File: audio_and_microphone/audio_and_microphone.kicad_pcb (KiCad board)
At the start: 2 copper layers, 17 x 15.5 mm, 12 parts

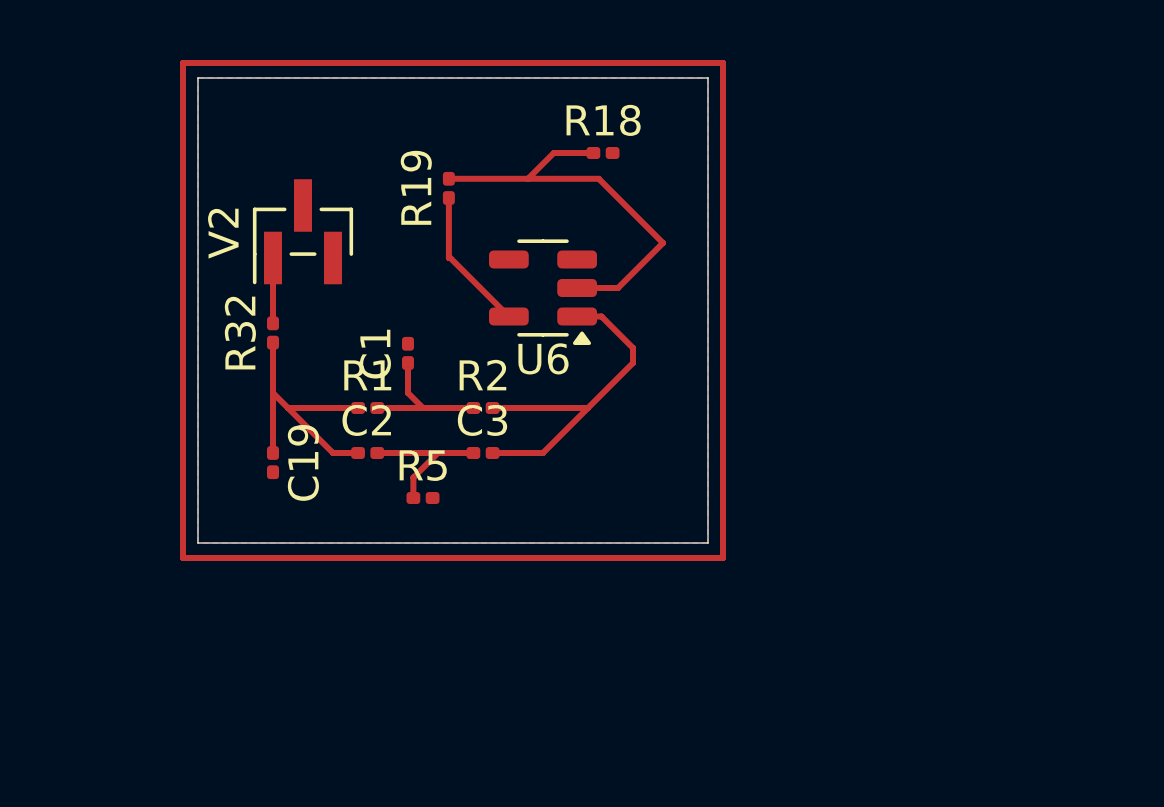
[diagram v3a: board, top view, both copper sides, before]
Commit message: pcb update with pin connectors
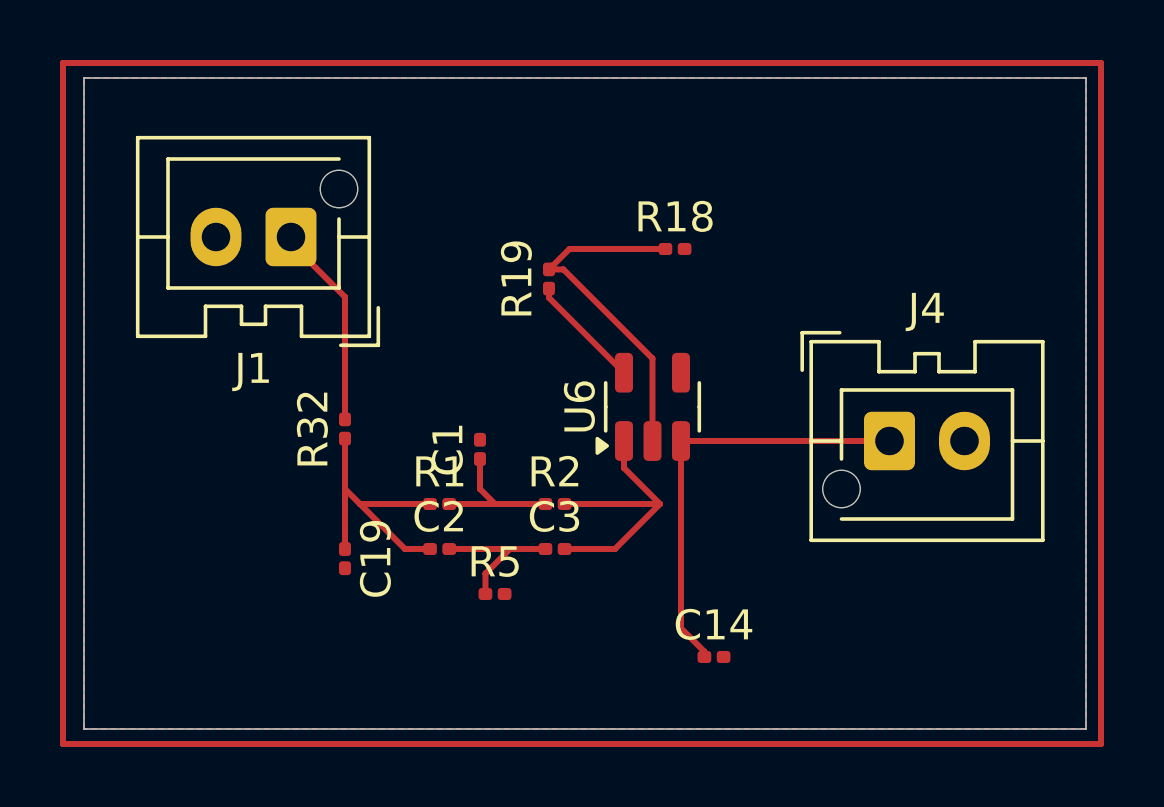
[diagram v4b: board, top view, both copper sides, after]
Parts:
- removed V2: VPWL, Connector_PinHeader_1.00mm:PinHeader_1x03_P1.00mm_Vertical_SMD_Pin1Left
- added C14: 0.1u, Capacitor_SMD:C_0201_0603Metric, F.Cu at (137.7, 64.8)
- added J1: Conn_01x02_Pin, Connector_JST:JST_XA_B02B-XASK-1-A_1x02_P2.50mm_Vertical, F.Cu at (123.6, 50.8)
- added J4: Conn_01x02_Pin, Connector_JST:JST_XA_B02B-XASK-1-A_1x02_P2.50mm_Vertical, F.Cu at (143.6, 57.6)
- moved U6 5.39 mm to (135.7, 56.5), turned to 90 degrees
- moved R19 4.50 mm to (132.2, 52.2)
- moved C1 4.00 mm to (129.9, 57.9)
- moved C19 4.00 mm to (125.4, 61.5)
- moved C2 4.00 mm to (128.6, 61.2)
- moved C3 4.00 mm to (132.4, 61.2)
- moved R1 4.00 mm to (128.6, 59.7)
- moved R18 4.00 mm to (136.4, 51.2)
- moved R2 4.00 mm to (132.4, 59.7)
- moved R32 4.00 mm to (125.4, 57.2)
- moved R5 4.00 mm to (130.4, 62.7)
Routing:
- net +3V3: track 0.00 -> 14.5 mm
- net Net-(J1-Pin_1): track 2.18 -> 6.83 mm
- net Net-(U6--): track 14.0 -> 11.6 mm
- net Net-(U6-+): track 11.9 -> 9.58 mm
- net /ENV_OUT: track 4.81 -> 3.84 mm
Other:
- board size 17 x 15.5 mm -> 33.4 x 21.7 mm

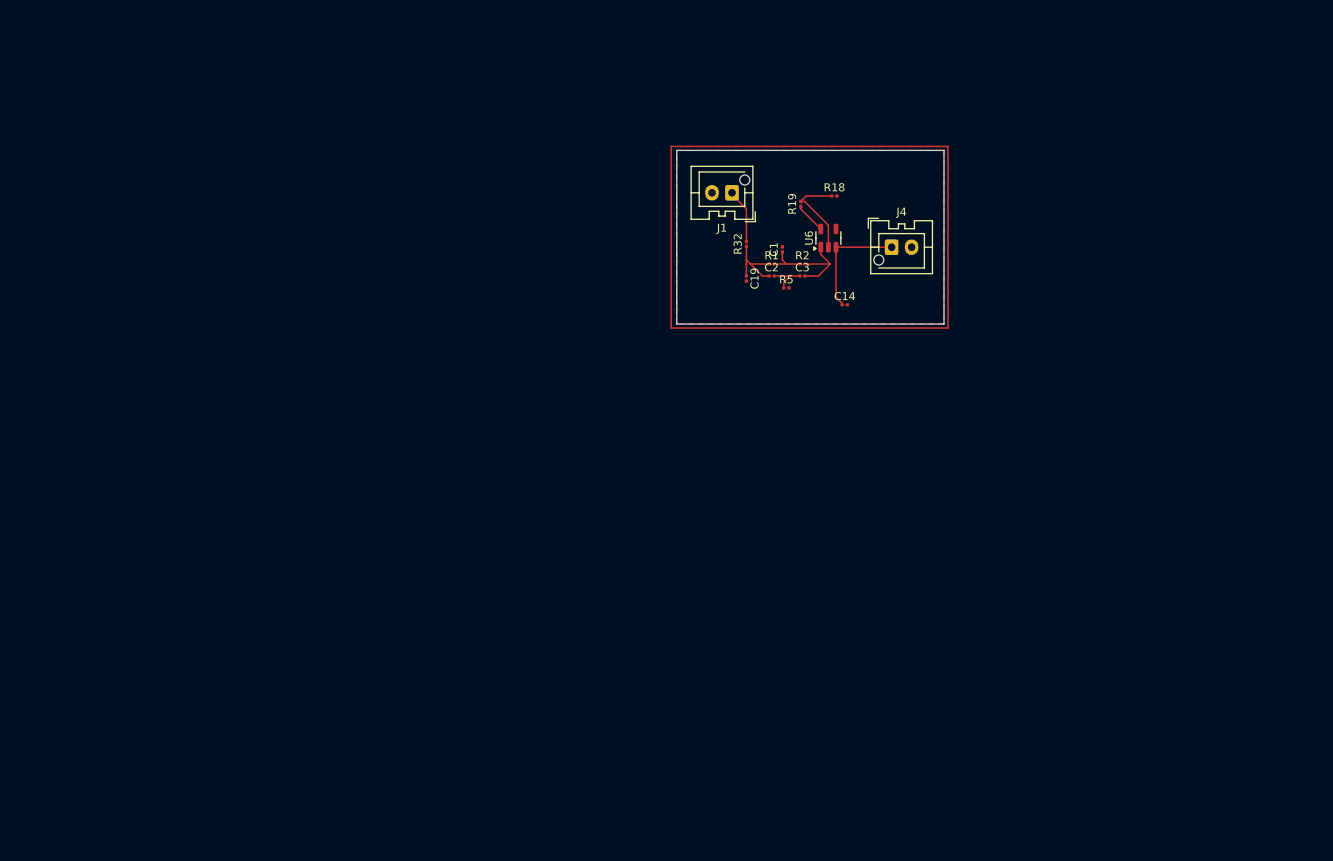
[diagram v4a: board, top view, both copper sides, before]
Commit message: pcb with vertical and horizontal male header pins lined up with arduino size
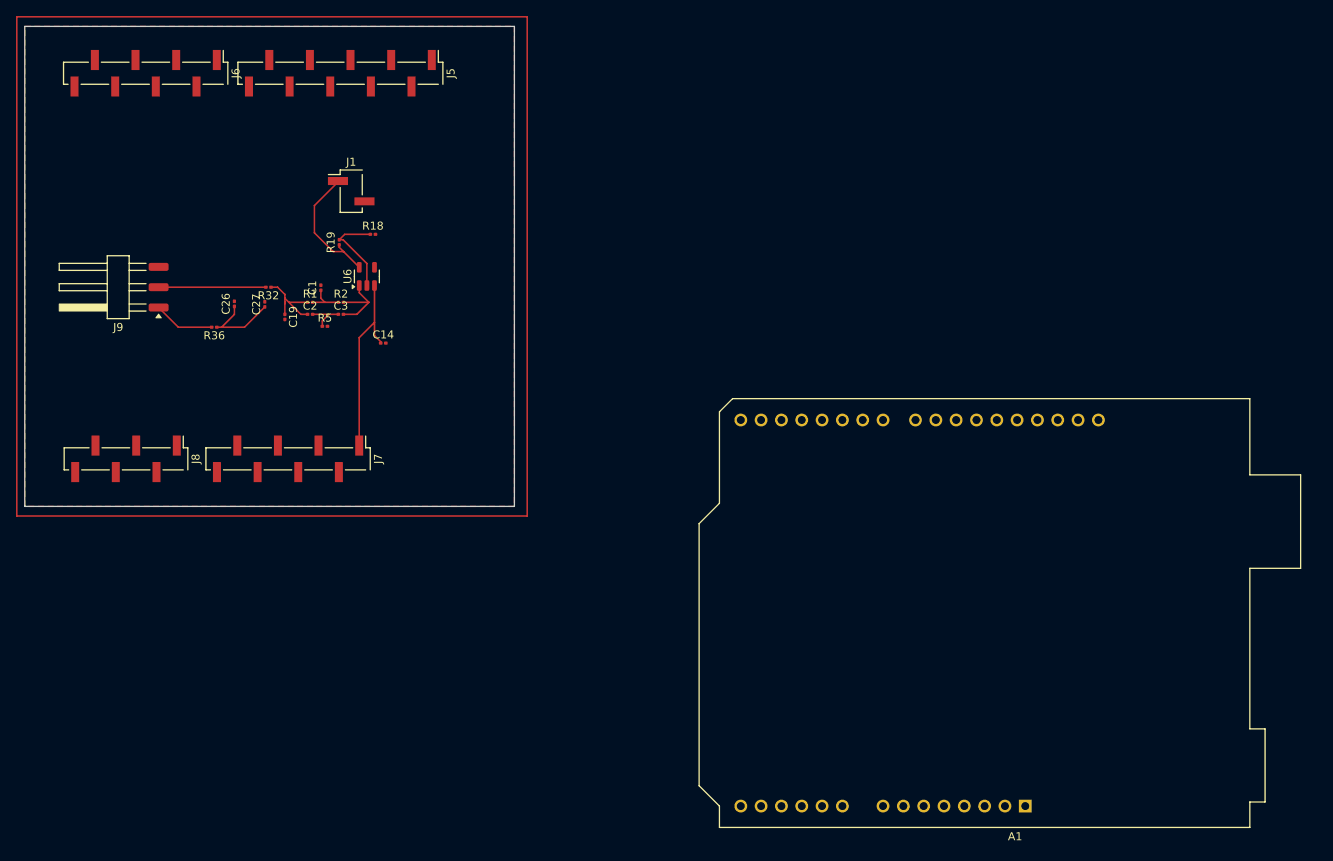
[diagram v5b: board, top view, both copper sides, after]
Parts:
- removed J4: Conn_01x02_Pin, Connector_JST:JST_XA_B02B-XASK-1-A_1x02_P2.50mm_Vertical
- added A1: Arduino_UNO_R3, Module:Arduino_UNO_R3, F.Cu at (160.3, 127.5)
- added C26: 0.1u, Capacitor_SMD:C_0201_0603Metric, F.Cu at (61.4, 64.7)
- added C27: 1.0u, Capacitor_SMD:C_0201_0603Metric, F.Cu at (65.2, 64.7)
- added J5: Conn_01x10_MountingPin, Connector_PinHeader_2.54mm:PinHeader_1x10_P2.54mm_Vertical_SMD_Pin1Left, F.Cu at (74.7, 35.9)
- added J6: Conn_01x08_MountingPin, Connector_PinHeader_2.54mm:PinHeader_1x08_P2.54mm_Vertical_SMD_Pin1Left, F.Cu at (50.3, 35.9)
- added J7: Conn_01x08_MountingPin, Connector_PinHeader_2.54mm:PinHeader_1x08_P2.54mm_Vertical_SMD_Pin1Left, F.Cu at (68.1, 84.1)
- added J8: Conn_01x06_MountingPin, Connector_PinHeader_2.54mm:PinHeader_1x06_P2.54mm_Vertical_SMD_Pin1Left, F.Cu at (47.9, 84.1)
- added J9: Conn_01x03_Pin, Connector_Harwin:Harwin_M20-89003xx_1x03_P2.54mm_Horizontal, F.Cu at (46.4, 62.6)
- added R36: 0, Resistor_SMD:R_0201_0603Metric, F.Cu at (58.9, 67.6)
- C1: value C -> 0.2u
- J1: value Conn_01x02_Pin -> Conn_01x01_MountingPin; footprint Connector_JST:JST_XA_B02B-XASK-1-A_1x02_P2.50mm_Vertical -> Connector_PinHeader_2.54mm:PinHeader_1x02_P2.54mm_Vertical_SMD_Pin1Left
- moved R32 60.0 mm to (65.7, 62.6), turned to 180 degrees
- moved C1 57.9 mm to (72.2, 62.7)
- moved C19 57.9 mm to (67.7, 66.3)
- moved C2 57.9 mm to (70.9, 66.0)
- moved C3 57.9 mm to (74.7, 66.0)
- moved R1 57.9 mm to (70.9, 64.5)
- moved R18 57.9 mm to (78.7, 56.0)
- moved R2 57.9 mm to (74.7, 64.5)
- moved R5 57.9 mm to (72.7, 67.5)
- moved U6 57.9 mm to (78.0, 61.3)
- moved C14 57.9 mm to (80.0, 69.6)
- moved R19 57.9 mm to (74.5, 57.0)
- moved J1 47.6 mm to (76.0, 50.6), turned to 0 degrees
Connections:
- J1 pad 1: Net-(J1-Pin_1) -> unconnected-(J1-Pin_1-Pad1)
- R32 pad 2: Net-(J1-Pin_1) -> input
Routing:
- net +3V3: track 14.5 -> 34.0 mm
- net input: track 0.00 -> 13.4 mm
- net /ENV_OUT: track 3.84 -> 16.2 mm
- net Net-(J9-Pin_1): track 0.00 -> 7.65 mm
- net Net-(J1-Pin_1): track 6.83 -> 0.00 mm
- net Net-(C19-Pad1): track 9.84 -> 10.8 mm
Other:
- board size 33.4 x 21.7 mm -> 61.2 x 60 mm

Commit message: old and new notch filter on schematic and pcb with switch connectors
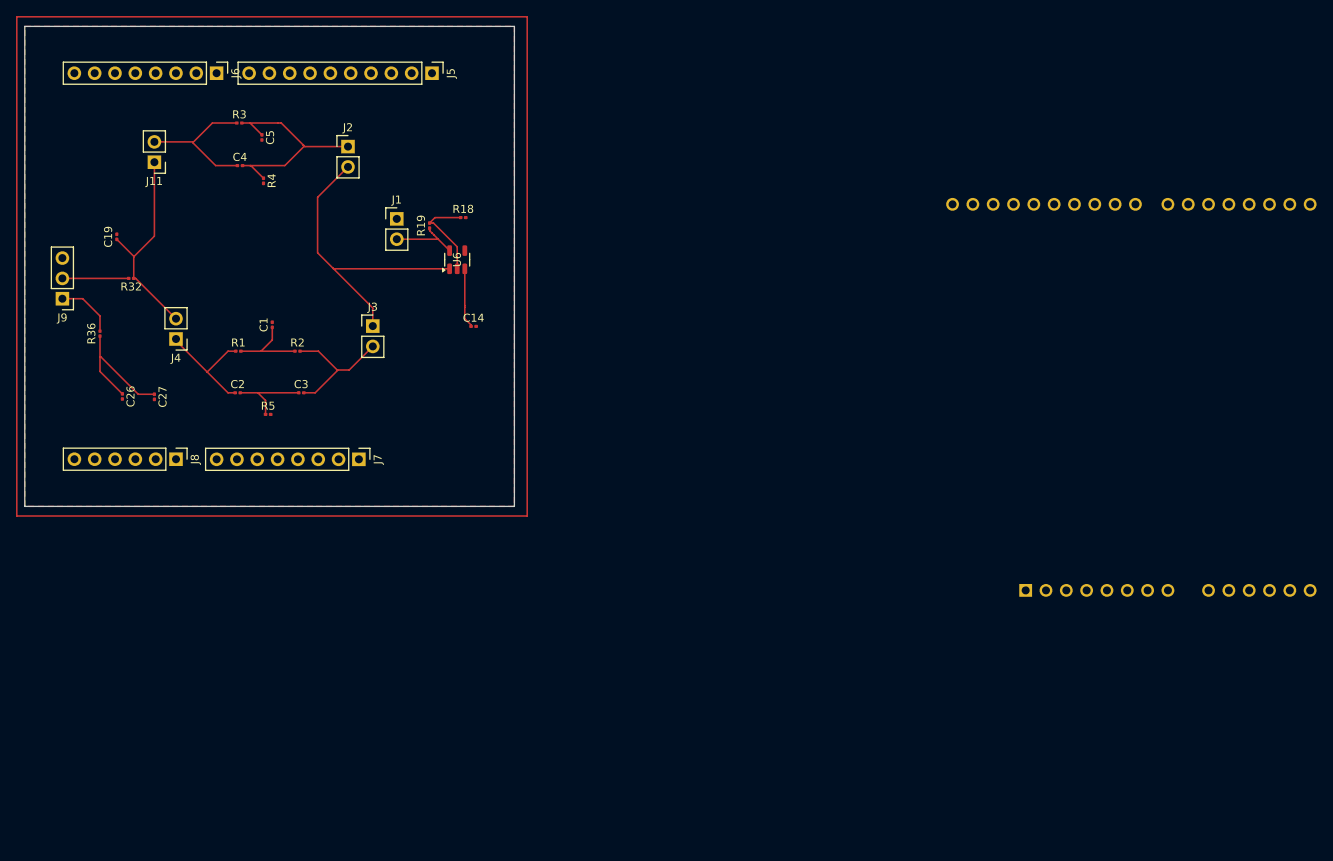
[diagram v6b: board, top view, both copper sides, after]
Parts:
- added C4: 0.1u, Capacitor_SMD:C_0201_0603Metric, F.Cu at (62.1, 47.4)
- added C5: 0.1u, Capacitor_SMD:C_0201_0603Metric, F.Cu at (64.8, 43.9)
- added J11: Conn_01x02, Connector_PinHeader_2.54mm:PinHeader_1x02_P2.54mm_Vertical, F.Cu at (51.4, 47.0)
- added J2: Conn_01x02, Connector_PinHeader_2.54mm:PinHeader_1x02_P2.54mm_Vertical, F.Cu at (75.6, 45.0)
- added J3: Conn_01x02, Connector_PinHeader_2.54mm:PinHeader_1x02_P2.54mm_Vertical, F.Cu at (78.7, 67.5)
- added J4: Conn_01x02, Connector_PinHeader_2.54mm:PinHeader_1x02_P2.54mm_Vertical, F.Cu at (54.1, 69.1)
- added R3: 150k, Resistor_SMD:R_0201_0603Metric, F.Cu at (62.0, 42.1)
- added R4: 10k, Resistor_SMD:R_0201_0603Metric, F.Cu at (65.0, 49.3)
- A1: moved to B.Cu
- J1: value Conn_01x01_MountingPin -> Conn_01x02; footprint Connector_PinHeader_2.54mm:PinHeader_1x02_P2.54mm_Vertical_SMD_Pin1Left -> Connector_PinHeader_2.54mm:PinHeader_1x02_P2.54mm_Vertical
- J5: footprint Connector_PinHeader_2.54mm:PinHeader_1x10_P2.54mm_Vertical_SMD_Pin1Left -> Connector_PinHeader_2.54mm:PinHeader_1x10_P2.54mm_Vertical
- J6, J7: footprint Connector_PinHeader_2.54mm:PinHeader_1x08_P2.54mm_Vertical_SMD_Pin1Left -> Connector_PinHeader_2.54mm:PinHeader_1x08_P2.54mm_Vertical
- J8: footprint Connector_PinHeader_2.54mm:PinHeader_1x06_P2.54mm_Vertical_SMD_Pin1Left -> Connector_PinHeader_2.54mm:PinHeader_1x06_P2.54mm_Vertical
- J9: footprint Connector_Harwin:Harwin_M20-89003xx_1x03_P2.54mm_Horizontal -> Connector_PinHeader_2.54mm:PinHeader_1x03_P2.54mm_Vertical
- moved A1 27.0 mm to (160.3, 100.5), turned to 0 degrees
- moved C19 23.3 mm to (46.7, 56.3), turned to 90 degrees
- moved C26 18.2 mm to (47.4, 76.3), turned to -90 degrees
- moved C27 18.0 mm to (51.4, 76.3), turned to -90 degrees
- moved R32 17.2 mm to (48.5, 61.5)
- moved R36 14.3 mm to (44.6, 68.4), turned to 90 degrees
- moved C2 13.3 mm to (61.8, 75.8)
- moved R5 13.1 mm to (65.6, 78.5)
- moved R18 11.5 mm to (90.0, 53.9)
- moved U6 11.5 mm to (89.2, 59.2)
- moved C14 11.5 mm to (91.3, 67.5)
- moved R19 11.5 mm to (85.8, 54.9)
- moved J5 11.5 mm to (86.1, 35.9)
- moved C3 11.0 mm to (69.8, 75.8)
- moved R1 10.9 mm to (61.9, 70.6)
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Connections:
- C19 pad 1: Net-(C19-Pad1) -> Net-(J11-Pin_1)
- C2 pad 1: Net-(C19-Pad1) -> Net-(J4-Pin_1)
- C3 pad 2: Net-(U6-+) -> Net-(J3-Pin_2)
- J1 pad 1: unconnected-(J1-Pin_1-Pad1) -> GND
- J1 pad 2: GND -> /ENV_OUT
- R1 pad 1: Net-(C19-Pad1) -> Net-(J4-Pin_1)
- R2 pad 2: Net-(U6-+) -> Net-(J3-Pin_2)
- R32 pad 1: Net-(C19-Pad1) -> Net-(J11-Pin_1)
- U6 pad 1: Net-(U6-+) -> Net-(J2-Pin_2)
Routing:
- net Net-(J2-Pin_2): track 0.00 -> 38.9 mm
- net Net-(J2-Pin_1): track 0.00 -> 27.8 mm
- net Net-(J11-Pin_1): track 0.00 -> 26.0 mm
- net Net-(J11-Pin_2): track 0.00 -> 18.1 mm
- net Net-(J3-Pin_2): track 0.00 -> 16.7 mm
- net Net-(J4-Pin_1): track 0.00 -> 15.0 mm
- net Net-(C19-Pad1): track 10.8 -> 0.00 mm
- net Net-(U6-+): track 9.58 -> 0.00 mm
- net +3V3: track 34.0 -> 24.6 mm
- net /ENV_OUT: track 16.2 -> 9.03 mm
- net Net-(C2-Pad2): track 5.04 -> 10.5 mm
- net Net-(C1-Pad1): track 4.91 -> 10.3 mm
- net input: track 13.4 -> 8.28 mm

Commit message: updated and imported footprints to match altium
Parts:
- C1, C14, C19, C2, C26, C27, C3, C4, C5: footprint Capacitor_SMD:C_0201_0603Metric -> C1608X5R1E105K080AC:CAPC1608X90N
- R1, R18, R19, R2, R3, R32, R36, R4, R5: footprint Resistor_SMD:R_0201_0603Metric -> RC0603FR_072KL:R0603
- moved A1 46.9 mm to (116.4, 84.1)
- moved J8 34.4 mm to (88.5, 84.1)
- moved J6 29.3 mm to (88.5, 35.9)
- moved J7 24.1 mm to (52.9, 84.1), turned to 90 degrees
- moved J5 19.5 mm to (66.6, 35.9)
- moved J11 5.80 mm to (51.4, 52.8)
- moved J2 5.23 mm to (75.5, 50.2)
- moved C26 4.22 mm to (47.8, 72.0), turned to 0 degrees
- moved R4 4.13 mm to (65.1, 53.4), turned to 0 degrees
- moved R18 4.10 mm to (89.8, 49.8), turned to 90 degrees
- moved C27 3.73 mm to (47.8, 77.1), turned to 0 degrees
- moved C4 3.20 mm to (61.4, 50.5)
- moved R3 3.12 mm to (62.0, 45.2), turned to 90 degrees
- moved R32 1.95 mm to (46.5, 61.5), turned to -90 degrees
- moved R19 1.91 mm to (87.4, 53.9), turned to 180 degrees
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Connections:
- J7 pad 1: unconnected-(J7-Pin_1-Pad1) -> +3V3
- J7 pad 6: unconnected-(J7-Pin_6-Pad6) -> GND
- J7 pad 7: unconnected-(J7-Pin_7-Pad7) -> GND
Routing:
- net Net-(J2-Pin_2): track 38.9 -> 32.0 mm
- net Net-(J11-Pin_1): track 26.0 -> 21.3 mm
- net +3V3: track 24.6 -> 27.6 mm
- net input: track 8.28 -> 5.89 mm
- net Net-(J9-Pin_1): track 7.47 -> 5.38 mm
- net Net-(J2-Pin_1): track 27.8 -> 29.8 mm
- net Net-(C1-Pad1): track 10.3 -> 8.55 mm
- net Net-(C2-Pad2): track 10.5 -> 8.98 mm

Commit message: fixed ground island in pcb
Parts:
- moved R5 18.6 mm to (60.8, 61.5), turned to 180 degrees
- moved J1 10.1 mm to (83.2, 44.1)
- moved C14 4.91 mm to (87.1, 70.0)
- moved J3 3.29 mm to (81.7, 66.1), turned to -90 degrees
- moved C1 3.15 mm to (66.1, 64.2)
- moved C2 3.15 mm to (62.3, 72.7)
- moved C3 3.15 mm to (69.5, 72.7)
- moved R1 3.15 mm to (62.5, 67.5)
- moved R2 3.15 mm to (69.0, 67.5)
- moved C5 2.89 mm to (67.7, 43.0)
- moved R3 2.89 mm to (64.8, 45.8)
- moved R4 2.89 mm to (67.9, 54.0)
- moved C4 2.89 mm to (64.2, 51.1)
- moved J11 2.88 mm to (54.2, 52.0), turned to 90 degrees
- moved J4 2.63 mm to (54.2, 66.5), turned to -90 degrees
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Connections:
- J7 pad 2: unconnected-(J7-Pin_2-Pad2) -> +3V3
- J7 pad 4: unconnected-(J7-Pin_4-Pad4) -> +3V3
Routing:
- net +3V3: track 27.6 -> 63.1 mm
- net Net-(J2-Pin_2): track 32.0 -> 11.4 mm
- net Net-(C2-Pad2): track 8.98 -> 17.8 mm
- net /ENV_OUT: track 9.39 -> 17.3 mm
- net Net-(J2-Pin_1): track 29.8 -> 28.6 mm
- net Net-(J11-Pin_1): track 21.3 -> 22.2 mm
- net Net-(J3-Pin_2): track 16.5 -> 17.2 mm
